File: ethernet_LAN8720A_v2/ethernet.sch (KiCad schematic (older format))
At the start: 46 parts, among them P1 SI-52003-F, P3 PoE, U1 LAN8720A-CP, U2 ASV-50.000MHZ-E-T

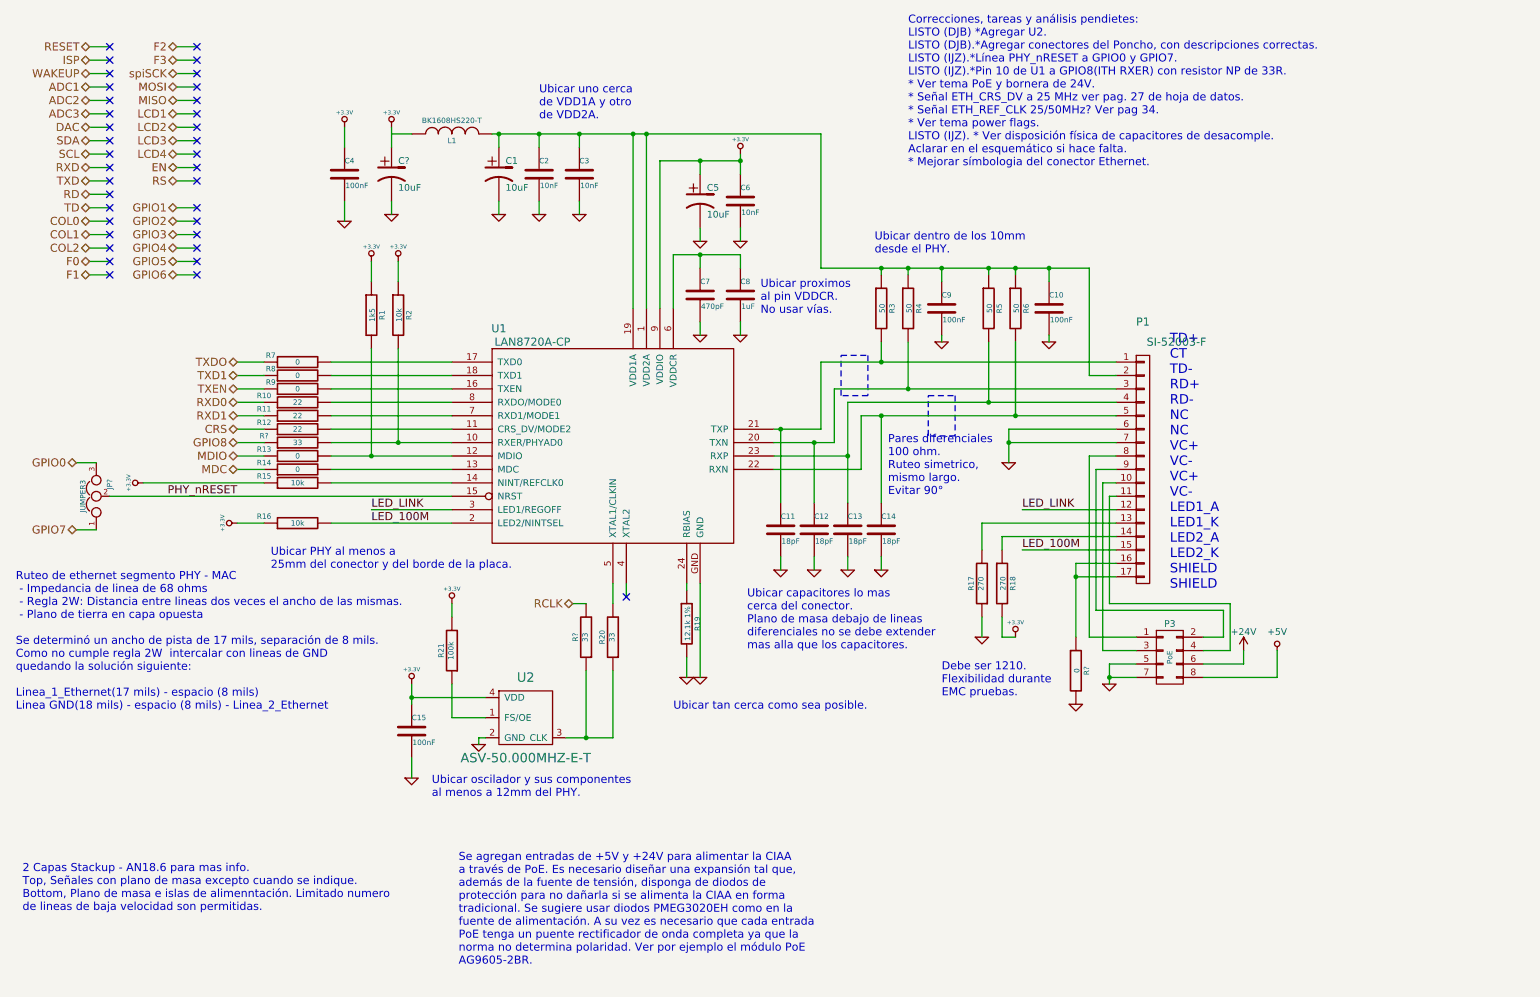
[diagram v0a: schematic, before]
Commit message: Se emprolija esquematico y comentarios
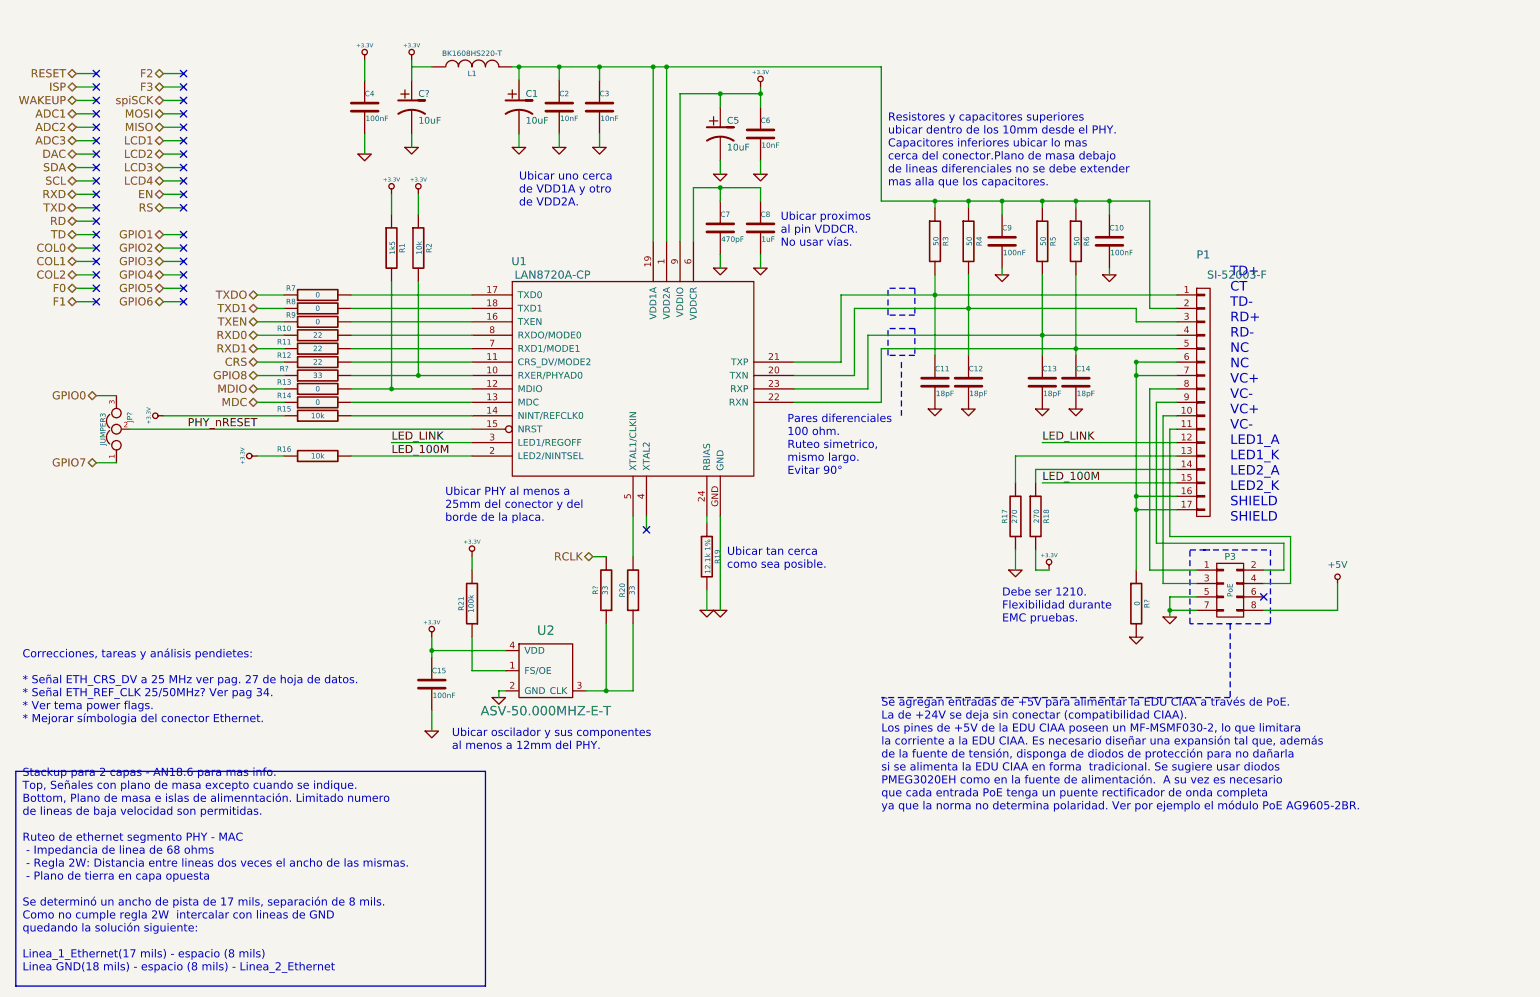
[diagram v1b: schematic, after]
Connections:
- net GND: no longer P1.6 (P6), P1.7 (P7)
- net at P1.16 (P16), P1.17 (P17), R?.1: now also P1.6 (P6), P1.7 (P7)
- net +24V: no longer names the net of P3.6 (P6)
- no-connect marks 36 -> 37
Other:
- note added: "Correcciones, tareas y análisis pendietes:\n\n* Señal ETH_CRS_DV a 25 MHz ver pag. 27 de hoja de datos.\n* Señal ETH_REF_CLK 25/50MHz? Ver pag 34.\n* Ver tema power flags.\n* Mejorar símbologia del conector Ethernet.\n"
- note added: "Resistores y capacitores superiores\nubicar dentro de los 10mm desde el PHY.\nCapacitores inferiores ubicar lo mas\ncerca del conector.Plano de masa debajo \nde lineas diferenciales no se debe extender\nmas alla que los capacitores."
- note added: "Se agregan entradas de +5V para alimentar la EDU CIAA a través de PoE. \nLa de +24V se deja sin conectar (compatibilidad CIAA).\nLos pines de +5V de la EDU CIAA poseen un MF-MSMF030-2, lo que limitara \nla corriente a la EDU CIAA. Es necesario diseñar una expansión tal que, además \nde la fuente de tensión, disponga de diodos de protección para no dañarla \nsi se alimenta la EDU CIAA en forma tra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"
- note added: "Stackup para 2 capas - AN18.6 para mas info.\nTop, Señales con plano de masa excepto cuando se indique.\nBottom, Plano de masa e islas de alimenntación. Limitado numero\nde lineas de baja velocidad son permitidas.\n\nRuteo de ethernet segmento PHY - MAC\n - Impedancia de linea de 68 ohms\n - Regla 2W: Distancia entre lineas dos veces el ancho de las mismas.\n - Plano de tierra en capa opuesta\n\n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"
- note added: "Ubicar PHY al menos a\n25mm del conector y del \nborde de la placa."
- note added: "Ubicar tan cerca \ncomo sea posible.\n"
- note removed: "2 Capas Stackup - AN18.6 para mas info.\nTop, Señales con plano de masa excepto cuando se indique.\nBottom, Plano de masa e islas de alimenntación. Limitado numero\nde lineas de baja velocidad son permitidas.\n"
- note removed: "Correcciones, tareas y análisis pendietes:\nLISTO (DJB) *Agregar U2.\nLISTO (DJB).*Agregar conectores del Poncho, con descripciones correctas.\nLISTO (IJZ).*Línea PHY_nRESET a GPIO0 y GPIO7.\nLISTO (IJZ).*Pin 10 de U1 a GPIO8(ITH RXER) con resistor NP de 33R.\n* Ver tema PoE y bornera de 24V.\n* Señal ETH_CRS_DV a 25 MHz ver pag. 27 de hoja de datos.\n* Señal ETH_REF_CLK 25/50MHz? Ver pag 34.\n* 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"
- note removed: "Ruteo de ethernet segmento PHY - MAC\n - Impedancia de linea de 68 ohms\n - Regla 2W: Distancia entre lineas dos veces el ancho de las mismas.\n - Plano de tierra en capa opuesta\n\nSe determinó un ancho de pista de 17 mils, separación de 8 mils.\nComo no cumple regla 2W intercalar con lineas de GND\nquedando la solución siguiente:\n\nLinea_1_Ethernet(17 mils) - espacio (8 mils)\nLinea GND(18 mil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"
- note removed: "Se agregan entradas de +5V y +24V para alimentar la CIAA\na través de PoE. Es necesario diseñar una expansión tal que, \nademás de la fuente de tensión, disponga de diodos de \nprotección para no dañarla si se alimenta la CIAA en forma \ntradicional. Se sugiere usar diodos PMEG3020EH como en la \nfuente de alimentación. A su vez es necesario que cada entrada\nPoE tenga un puente rectificador de o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"
- note removed: "Ubicar PHY al menos a\n25mm del conector y del borde de la placa."
- note removed: "Ubicar capacitores lo mas\ncerca del conector.\nPlano de masa debajo de lineas \ndiferenciales no se debe extender\nmas alla que los capacitores."
- note removed: "Ubicar dentro de los 10mm\ndesde el PHY."
- note removed: "Ubicar tan cerca como sea posible.\n"
- moved on the sheet: C1, C10, C11, C12, C13, C14, C15, C2, C3, C4, C5, C6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

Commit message: Numeración, corrección de nombres de etiquetas de jerarquía (letra o por cero), pasa el ERC.
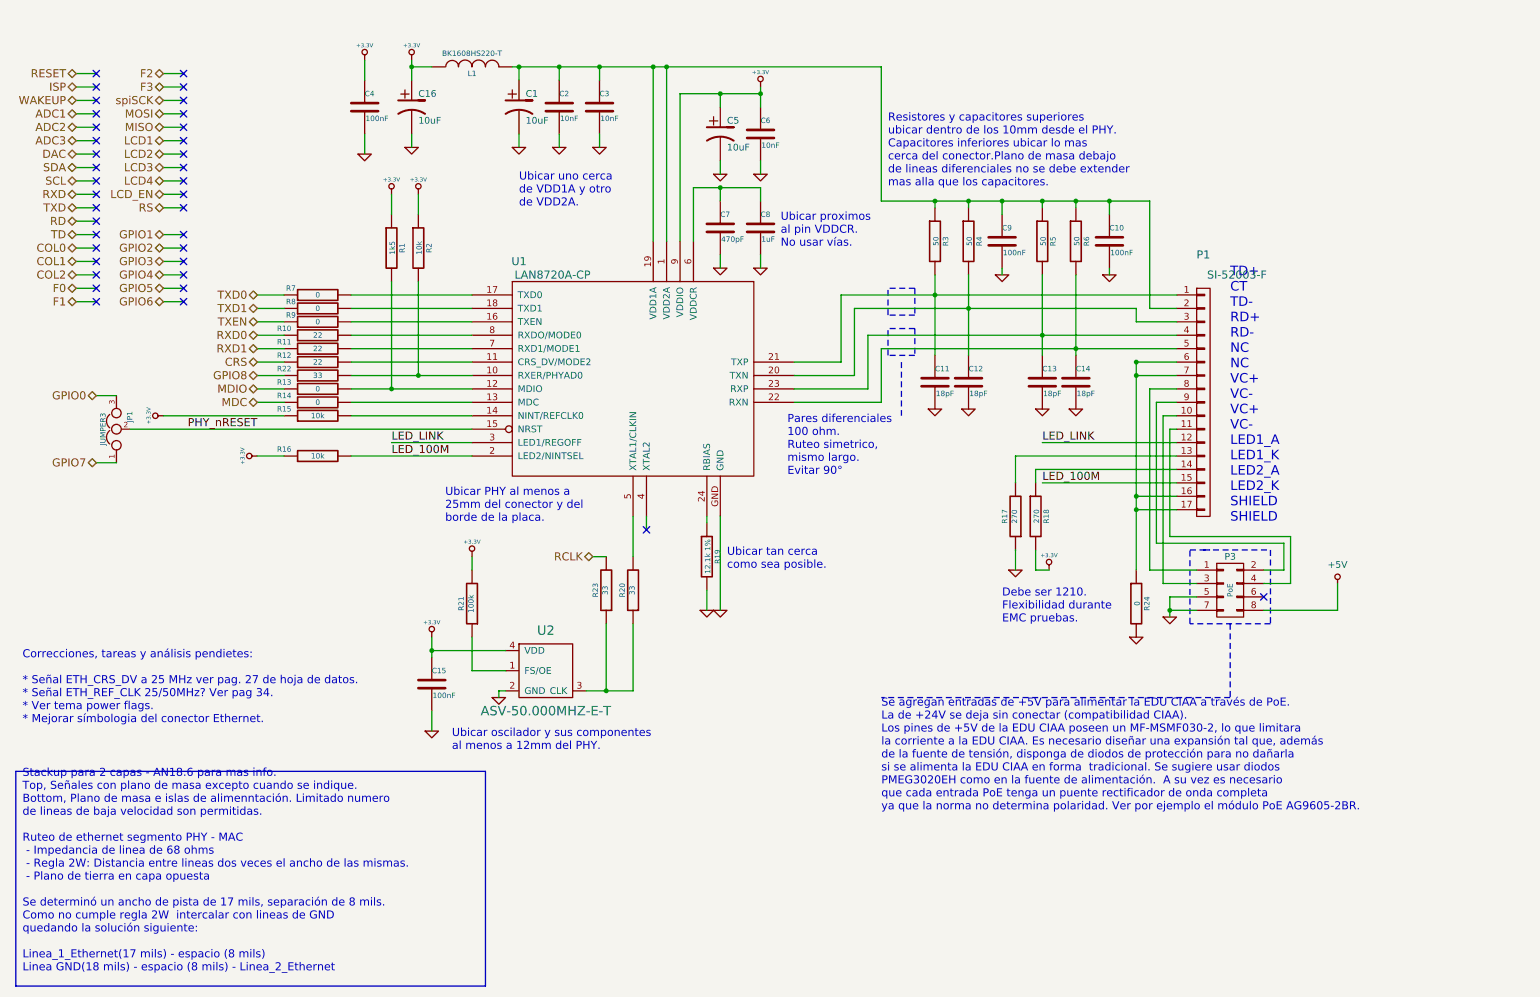
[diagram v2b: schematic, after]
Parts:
- gave numbers to parts that had none: 5
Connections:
- net +3.3V: now also L1.1
- net TXDO renamed TXD0

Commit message: Asocio footprints y realizo un placement MUY preliminar.
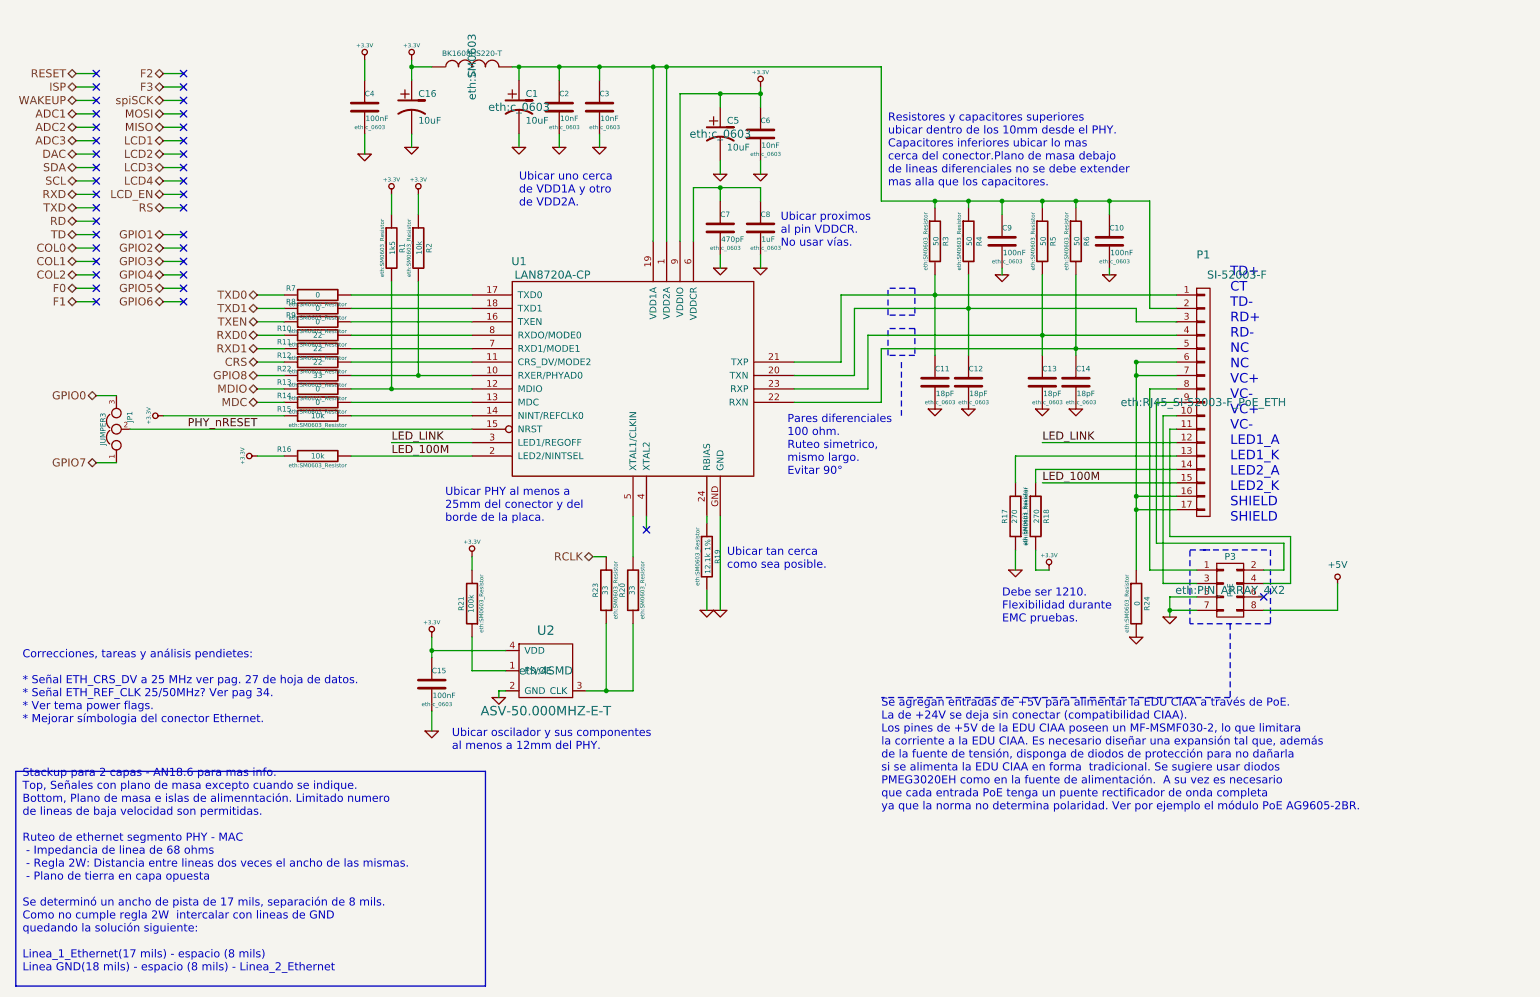
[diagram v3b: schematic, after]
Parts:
- C1, C10, C11, C12, C13, C14, C15, C2, C3, C4, C5, C6, C7, C8, C9: footprint ~ -> eth:c_0603
- C16: footprint ~ -> (none)
- L1: footprint ~ -> eth:SM0603
- P1: footprint ~ -> eth:RJ45_SI-52003-F_PoE_ETH
- P3: footprint ~ -> eth:PIN_ARRAY_4X2
- R1, R10, R11, R12, R13, R14, R15, R16, R17, R18, R19, R2, R20, R21, R22, R23, R24, R3, R4, R5, R6, R7, R8, R9: footprint ~ -> eth:SM0603_Resistor
- U1: footprint (none) -> eth:QFN24
- U2: footprint ~ -> eth:4SMD

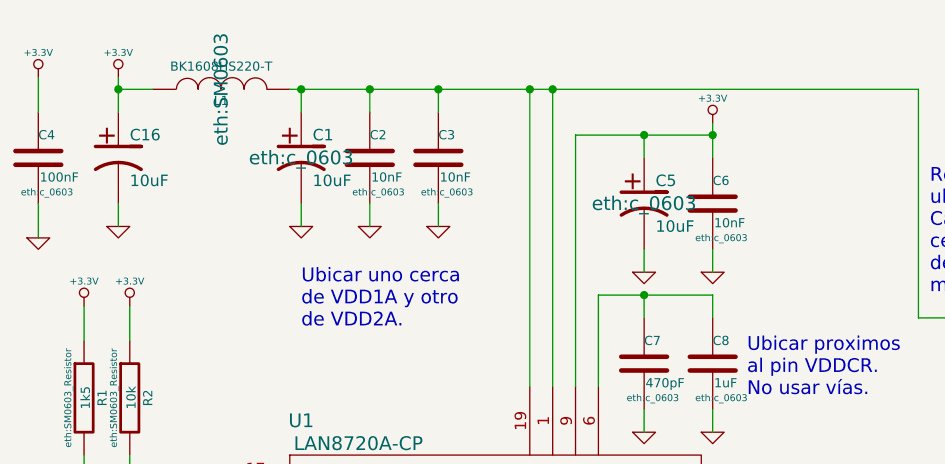
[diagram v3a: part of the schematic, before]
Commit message: Agrego 1206 para capacitor, corrijo asignación capas de 10uF.
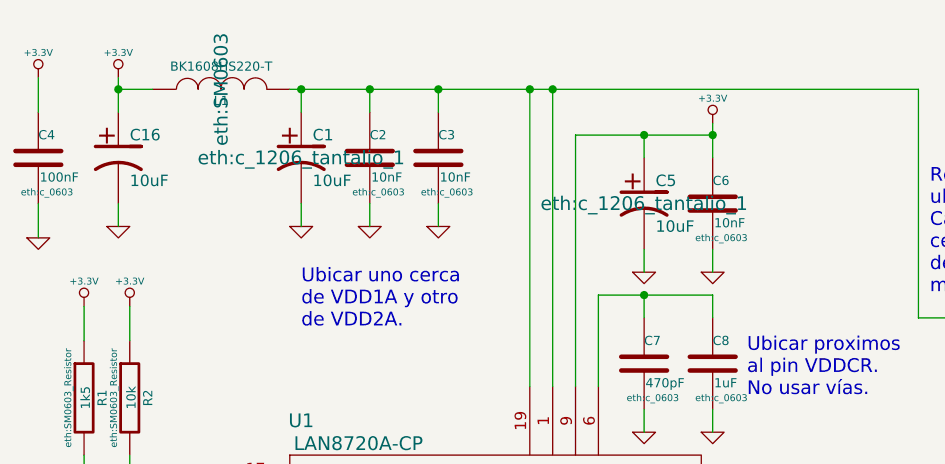
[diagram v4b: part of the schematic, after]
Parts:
- C1, C5: footprint eth:c_0603 -> eth:c_1206_tantalio_1
- C16: footprint (none) -> eth:c_1206_tantalio_1
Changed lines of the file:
@@
 F 0 "C5" H 5850 1500 50  0000 L CNN
 F 1 "10uF" H 5850 1300 50  0000 L CNN
-F 2 "eth:c_0603" H 5800 1400 60  0000 C CNN
+F 2 "eth:c_1206_tantalio_1" H 5800 1400 60  0000 C CNN
 F 3 "~" H 5800 1400 60  0000 C CNN
 	1    5800 1400
@@
 F 0 "C1" H 4350 1300 50  0000 L CNN
 F 1 "10uF" H 4350 1100 50  0000 L CNN
-F 2 "eth:c_0603" H 4300 1200 60  0000 C CNN
+F 2 "eth:c_1206_tantalio_1" H 4300 1200 60  0000 C CNN
 F 3 "~" H 4300 1200 60  0000 C CNN
 	1    4300 1200
@@
 F 0 "C16" H 3550 1300 50  0000 L CNN
 F 1 "10uF" H 3550 1100 50  0000 L CNN
-F 2 "" H 3500 1200 60  0001 C CNN
+F 2 "eth:c_1206_tantalio_1" H 3500 1200 60  0001 C CNN
 F 3 "~" H 3500 1200 60  0000 C CNN
 	1    3500 1200

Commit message: Nombre de lineas de esquemáticos.
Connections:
- net Tx_N: now reaches C12.1, P1.3 (P3), R4.2, U1.20 (TXN)
- net Tx_P: now reaches C11.1, P1.1 (P1), R3.2, U1.21 (TXP)
- net Rx_N: now reaches C14.1, P1.5 (P5), R6.2, U1.22 (RXN)
- net Rx_P: now reaches C13.1, P1.4 (P4), R5.2, U1.23 (RXP)
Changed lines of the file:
@@
 F 0 "P1" H 9400 4500 60  0000 C CNN
 F 1 "SI-52003-F" H 9650 4350 60  0000 C CNN
-F 2 "eth:RJ45_SI-52003-F_PoE_ETH" H 9400 3400 60  0000 C CNN
+F 2 "eth:RJ45_SI-52003-F_PoE_ETH" V 9500 3400 60  0000 C CNN
 F 3 "~" H 9400 3400 60  0000 C CNN
 	1    9400 3400
@@
 	9900 5050 9300 5050
 Connection ~ 3500 900
+Text Label 7750 2600 0    60   ~ 0
+Tx_P
+Text Label 7750 2700 0    60   ~ 0
+Tx_N
+Text Label 7750 2900 0    60   ~ 0
+Rx_P
+Text Label 7750 3000 0    60   ~ 0
+Rx_N
 $EndSCHEMATC
